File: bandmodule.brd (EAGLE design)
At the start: 35.5 x 41.3 mm, 15 parts

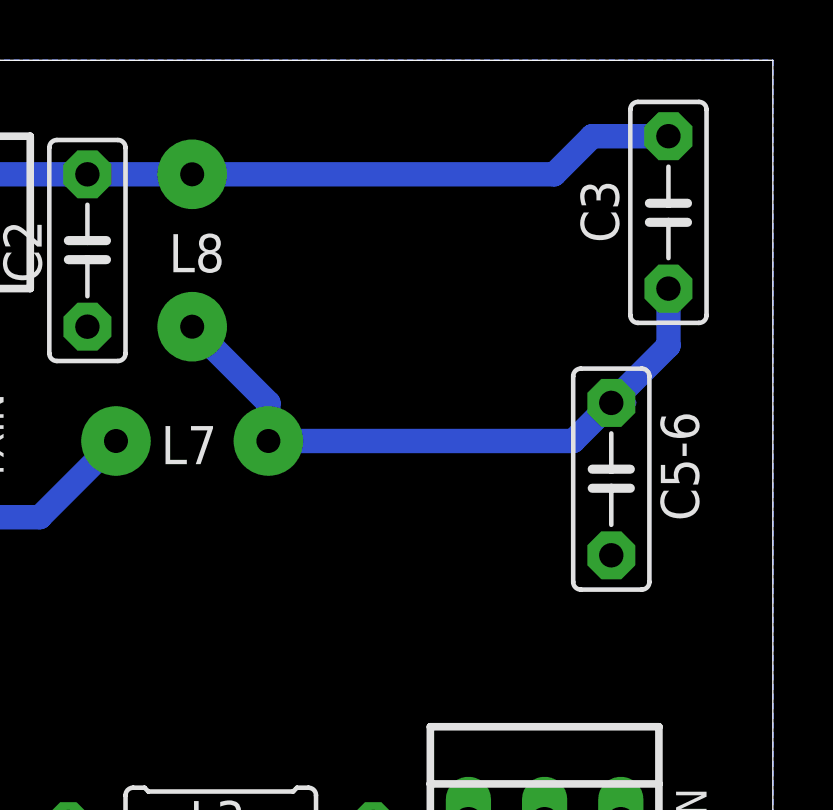
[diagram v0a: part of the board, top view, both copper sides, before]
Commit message: Made traces shorter
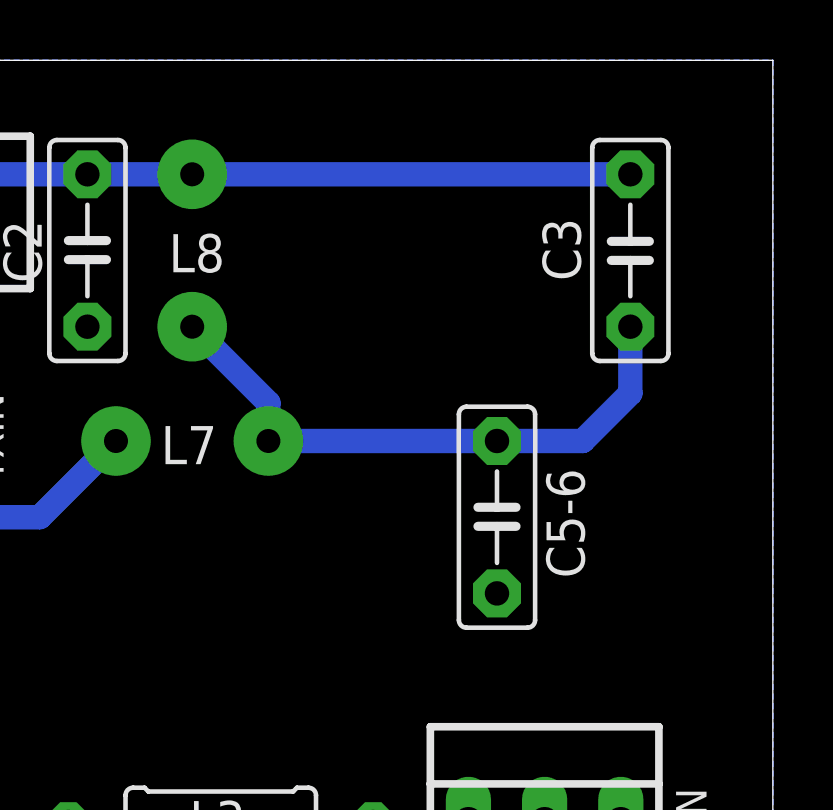
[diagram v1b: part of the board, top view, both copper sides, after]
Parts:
- moved C5-6 4.02 mm to (26.4, 26.0)
- moved C3 1.80 mm to (30.8, 34.9)
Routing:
- net N$5: track 22.1 -> 19.8 mm
- net N$8: track 25.0 -> 23.2 mm
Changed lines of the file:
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@@
 <attribute name="NAME" x="11.176" y="33.8455" size="1.27" layer="25" ratio="10" rot="R90"/>
 </element>
-<element name="C3" library="capacitor-wima" package="C5B2.5" value="33p" x="32.0675" y="36.195" smashed="yes" rot="R270">
-<attribute name="NAME" x="29.1465" y="37.2745" size="1.27" layer="25" ratio="10" rot="R270"/>
+<element name="C3" library="capacitor-wima" package="C5B2.5" value="33p" x="30.7975" y="34.925" smashed="yes" rot="R270">
+<attribute name="NAME" x="27.8765" y="36.0045" size="1.27" layer="25" ratio="10" rot="R270"/>
 </element>
 <element name="C31" library="capacitor-wima" package="C5B2.5" value="5p" x="17.145" y="12.065" smashed="yes">
 <attribute name="NAME" x="10.033" y="10.0965" size="1.27" layer="25" ratio="10"/>
 </element>
-<element name="C5-6" library="capacitor-wima" package="C5B2.5" value="330p" x="30.1625" y="27.305" smashed="yes" rot="R90">
-<attribute name="NAME" x="33.0835" y="25.908" size="1.27" layer="25" ratio="10" rot="R90"/>
+<element name="C5-6" library="capacitor-wima" package="C5B2.5" value="330p" x="26.3525" y="26.035" smashed="yes" rot="R90">
+<attribute name="NAME" x="29.2735" y="24.003" size="1.27" layer="25" ratio="10" rot="R90"/>
 </element>
 <element name="CT1" library="rcl" package="CTRIMTZ03" value="60p" x="6.35" y="13.335" smashed="yes" rot="R90">
@@
 <contactref element="C5-6" pad="2"/>
 <contactref element="C3" pad="2"/>
-<wire x1="30.7975" y1="29.845" x2="30.1625" y2="29.845" width="0.4064" layer="16"/>
 <contactref element="L8" pad="P$1"/>
 <contactref element="L7" pad="P$2"/>
-<wire x1="32.0675" y1="33.655" x2="32.0675" y2="31.75" width="0.8128" layer="16"/>
-<wire x1="32.0675" y1="31.75" x2="30.1625" y2="29.845" width="0.8128" layer="16"/>
-<wire x1="30.1625" y1="29.845" x2="28.8925" y2="28.575" width="0.8128" layer="16"/>
-<wire x1="18.7325" y1="28.575" x2="28.8925" y2="28.575" width="0.8128" layer="16"/>
 <wire x1="16.1925" y1="32.385" x2="18.7325" y2="29.845" width="0.8128" layer="16"/>
-<wire x1="18.7325" y1="29.845" x2="18.7325" y2="28.575" width="0.8128" layer="16"/>
+<wire x1="18.7325" y1="28.575" x2="18.7325" y2="29.845" width="0.8128" layer="16"/>
+<wire x1="30.7975" y1="32.385" x2="30.7975" y2="30.1625" width="0.8128" layer="16"/>
+<wire x1="30.7975" y1="30.1625" x2="29.21" y2="28.575" width="0.8128" layer="16"/>
+<wire x1="29.21" y1="28.575" x2="26.3525" y2="28.575" width="0.8128" layer="16"/>
+<wire x1="26.3525" y1="28.575" x2="18.7325" y2="28.575" width="0.8128" layer="16"/>
 </signal>
 <signal name="N$6">
@@
 <wire x1="12.7" y1="37.465" x2="16.1925" y2="37.465" width="0.8128" layer="16"/>
 <wire x1="7.62" y1="37.465" x2="12.7" y2="37.465" width="0.8128" layer="16"/>
-<wire x1="16.1925" y1="37.465" x2="28.2575" y2="37.465" width="0.8128" layer="16"/>
-<wire x1="28.2575" y1="37.465" x2="29.5275" y2="38.735" width="0.8128" layer="16"/>
-<wire x1="29.5275" y1="38.735" x2="32.0675" y2="38.735" width="0.8128" layer="16"/>
+<wire x1="16.1925" y1="37.465" x2="30.7975" y2="37.465" width="0.8128" layer="16"/>
 </signal>
 </signals>
